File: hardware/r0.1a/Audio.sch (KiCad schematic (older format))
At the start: 76 parts, among them J4 MBIAS, J5 TX_Trim, J6 Kenwood-2.5, J7 Radio, J8 Kenwood-3.5, Q1 IRLML2060, U5 LM386, U6 MCP6002-xSN, U7 MCP6002-xSN, U8 LMV341

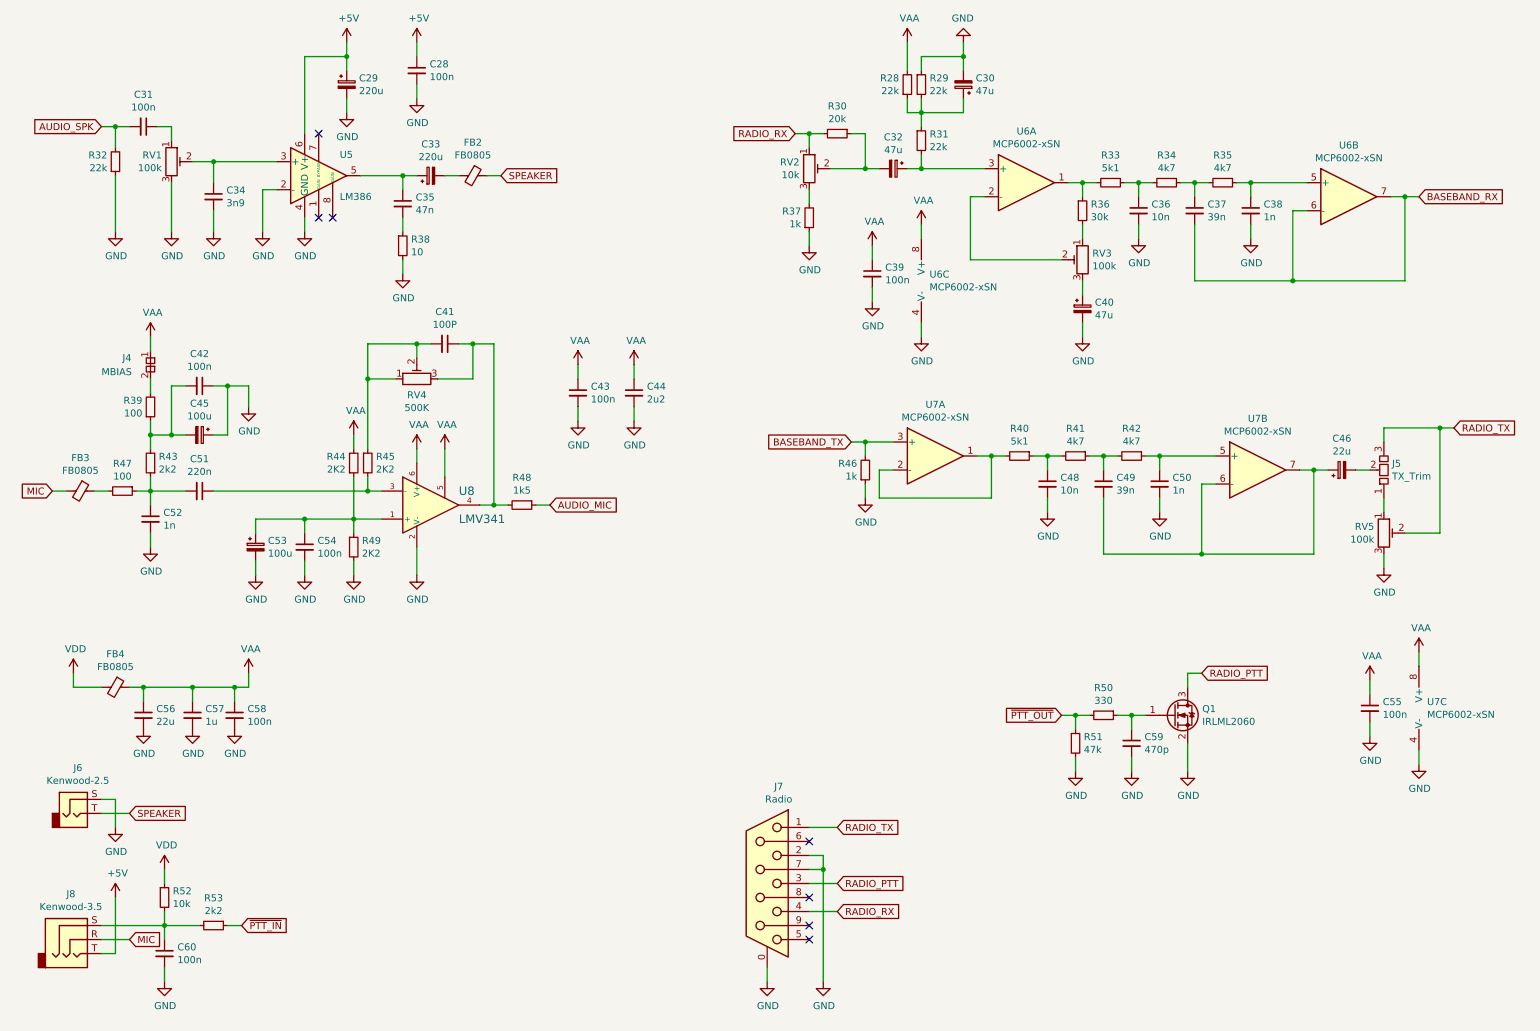
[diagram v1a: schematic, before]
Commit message: Small fixes / updates
* Fixed library path
* Added 12 MHz TCXO
* Replaced rotary encoder with more buttons
* Changed radio connector pinout to be compatible with Repeater Builder and BI7JTA modem boards
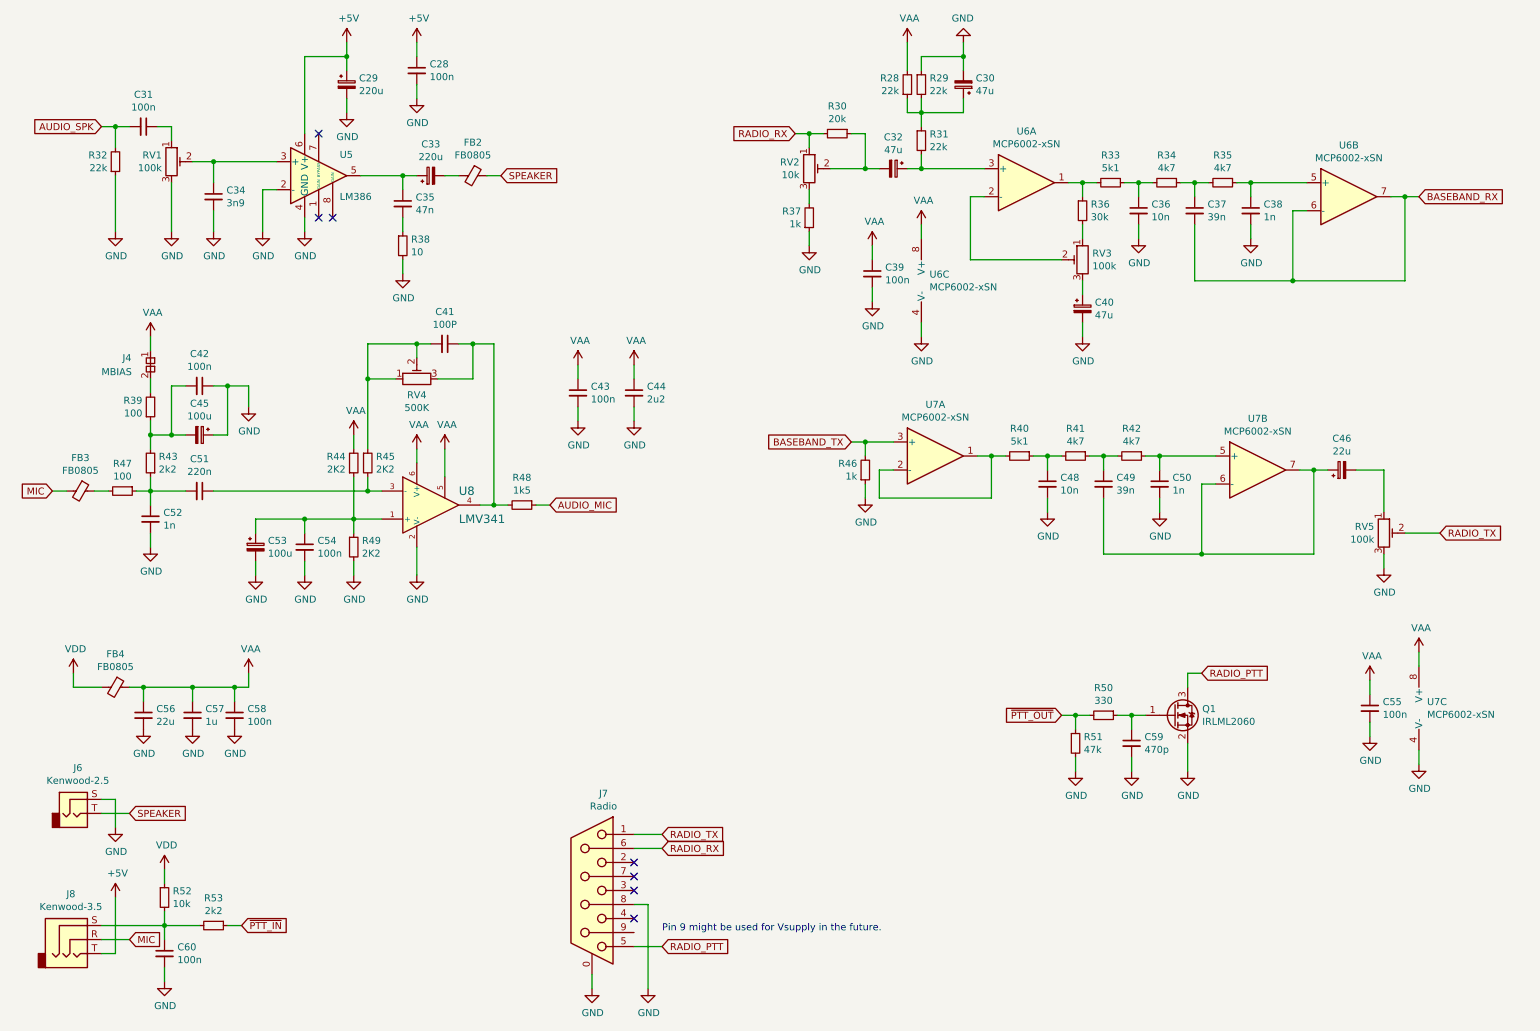
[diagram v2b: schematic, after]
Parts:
- removed J5: TX_Trim, symbol pkl_misc:pkl_double_jumper
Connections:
- net GND: now also J7.8; no longer J7.2, J7.7
- net RADIO_PTT: now also J7.5; no longer J7.3
- net RADIO_RX: now also J7.6; no longer J7.4
- net at C46.2: now also RV5.1
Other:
- note added: "Pin 9 might be used for Vsupply in the future."
- moved on the sheet: J7
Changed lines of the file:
@@
 	9750 3850 9850 3850
 Connection ~ 9750 3850
-Wire Wire Line
-	10050 3850 10150 3850
-$Comp
-L pkl_misc:pkl_double_jumper J5
-U 1 1 6210D6B9
-P 10250 3850
-F 0 "J5" V 10296 3792 50  0000 R CNN
-F 1 "TX_Trim" V 10205 3792 50  0000 R CNN
-F 2 "" H 10200 3850 50  0001 C CNN
-F 3 "" H 10200 3850 50  0001 C CNN
-	1    10250 3850
-	0    -1   -1   0
-$EndComp
 $Comp
 L Device:R_POT_TRIM RV5
@@
 	1    0    0    -1
 $EndComp
-Wire Wire Line
-	10250 4050 10250 4150
 $Comp
 L power:GND #PWR093
@@
 	10250 4550 10250 4450
 Wire Wire Line
-	10250 3650 10250 3550
-Wire Wire Line
-	10250 3550 10650 3550
-Wire Wire Line
-	10650 3550 10650 4300
-Wire Wire Line
 	10650 4300 10400 4300
-Wire Wire Line
-	10650 3550 10750 3550
-Connection ~ 10650 3550
-Text GLabel 10750 3550 2    50   Input ~ 0
+Text GLabel 10650 4300 2    50   Input ~ 0
 RADIO_TX
 $Comp
@@
 L Connector:DB9_Female_MountingHoles J7
 U 1 1 62239A82
-P 5850 6800
-F 0 "J7" H 5768 7492 50  0000 C CNN
-F 1 "Radio" H 5768 7401 50  0000 C CNN
-F 2 "" H 5850 6800 50  0001 C CNN
-F 3 " ~" H 5850 6800 50  0001 C CNN
-	1    5850 6800
+P 4600 6850
+F 0 "J7" H 4518 7542 50  0000 C CNN
+F 1 "Radio" H 4518 7451 50  0000 C CNN
+F 2 "" H 4600 6850 50  0001 C CNN
+F 3 " ~" H 4600 6850 50  0001 C CNN
+	1    4600 6850
 	-1   0    0    -1
 $EndComp
@@
 L power:GND #PWR0114
 U 1 1 62239ED8
-P 5850 7500
-F 0 "#PWR0114" H 5850 7250 50  0001 C CNN
-F 1 "GND" H 5855 7327 50  0000 C CNN
-F 2 "" H 5850 7500 50  0001 C CNN
-F 3 "" H 5850 7500 50  0001 C CNN
-	1    5850 7500
-	1    0    0    -1
-$EndComp
-Wire Wire Line
-	5850 7400 5850 7500
-Text GLabel 6350 6400 2    50   Input ~ 0
+P 4600 7550
+F 0 "#PWR0114" H 4600 7300 50  0001 C CNN
+F 1 "GND" H 4605 7377 50  0000 C CNN
+F 2 "" H 4600 7550 50  0001 C CNN
+F 3 "" H 4600 7550 50  0001 C CNN
+	1    4600 7550
+	1    0    0    -1
+$EndComp
+Wire Wire Line
+	4600 7450 4600 7550
+Text GLabel 5100 6450 2    50   Input ~ 0
 RADIO_TX
-Wire Wire Line
-	6150 6600 6250 6600
-Wire Wire Line
-	6250 6600 6250 6700
-Wire Wire Line
-	6250 6700 6150 6700
-Wire Wire Line
-	6250 6700 6250 7500
-Connection ~ 6250 6700
 $Comp
 L power:GND #PWR0115
 U 1 1 62267D15
-P 6250 7500
-F 0 "#PWR0115" H 6250 7250 50  0001 C CNN
-F 1 "GND" H 6255 7327 50  0000 C CNN
-F 2 "" H 6250 7500 50  0001 C CNN
-F 3 "" H 6250 7500 50  0001 C CNN
-	1    6250 7500
-	1    0    0    -1
-$EndComp
-NoConn ~ 6150 6500
-NoConn ~ 6150 6900
-NoConn ~ 6150 7100
-NoConn ~ 6150 7200
-Text GLabel 6350 6800 2    50   Input ~ 0
+P 5000 7550
+F 0 "#PWR0115" H 5000 7300 50  0001 C CNN
+F 1 "GND" H 5005 7377 50  0000 C CNN
+F 2 "" H 5000 7550 50  0001 C CNN
+F 3 "" H 5000 7550 50  0001 C CNN
+	1    5000 7550
+	1    0    0    -1
+$EndComp
+Text GLabel 5100 7250 2    50   Input ~ 0
 RADIO_PTT
-Wire Wire Line
-	6150 6400 6350 6400
-Text GLabel 6350 7000 2    50   Input ~ 0
+Text GLabel 5100 6550 2    50   Input ~ 0
 RADIO_RX
 Wire Wire Line
-	6350 7000 6150 7000
-Wire Wire Line
-	6350 6800 6150 6800
-Wire Wire Line
 	6850 800  6850 1000
+Wire Wire Line
+	10050 3850 10250 3850
+Wire Wire Line
+	10250 3850 10250 4150
+Wire Wire Line
+	4900 6950 5000 6950
+Wire Wire Line
+	5000 6950 5000 7550
+Wire Wire Line
+	4900 7250 5100 7250
+Wire Wire Line
+	4900 6550 5100 6550
+Wire Wire Line
+	4900 6450 5100 6450
+NoConn ~ 4900 6650
+NoConn ~ 4900 6750
+NoConn ~ 4900 6850
+NoConn ~ 4900 7050
+Text Notes 5100 7150 0    50   ~ 0
+Pin 9 might be used for Vsupply in the future.
 $EndSCHEMATC

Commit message: Replaced Xtal parallel R with series R
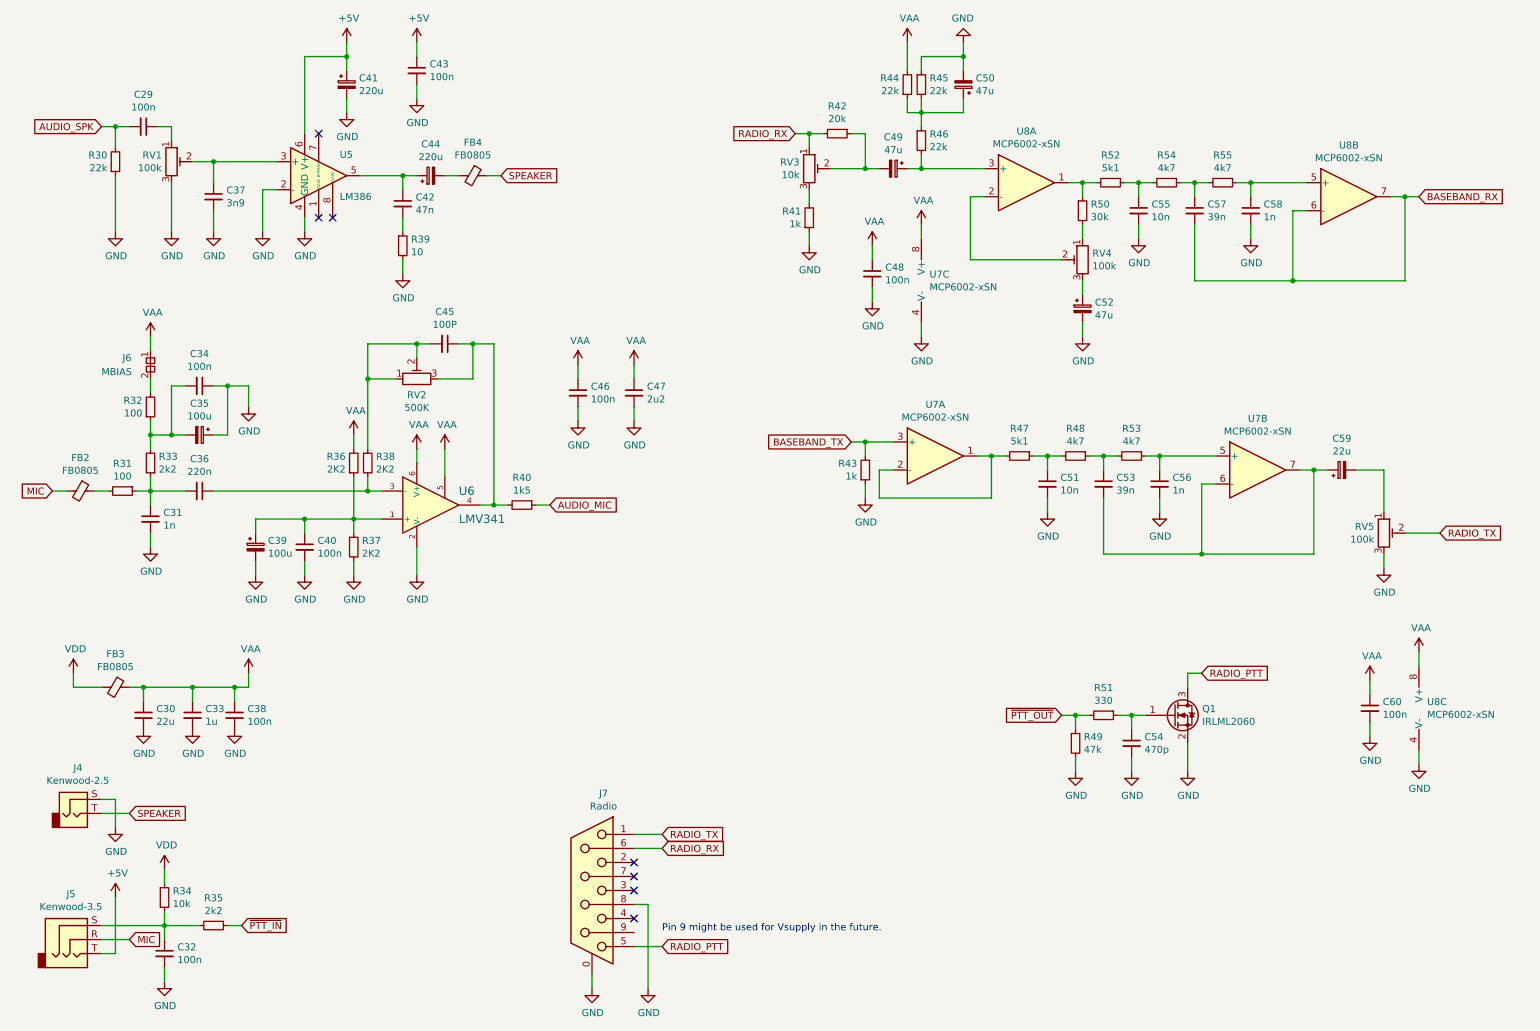
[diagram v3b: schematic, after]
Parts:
- renumbered C31 to C29, C56 to C30, C52 to C31, C60 to C32, C57 to C33, C42 to C34, C45 to C35, C51 to C36, C34 to C37, C58 to C38, C53 to C39, C54 to C40, C29 to C41, C35 to C42, C28 to C43, C33 to C44, C41 to C45, C43 to C46, C44 to C47, C39 to C48, C32 to C49, C30 to C50, C48 to C51, C40 to C52, C49 to C53, C59 to C54, C36 to C55, C50 to C56, C37 to C57, C38 to C58, C46 to C59, C55 to C60, FB3 to FB2, FB4 to FB3, FB2 to FB4, J6 to J4, J8 to J5, J4 to J6, R32 to R30, R47 to R31, R39 to R32, R43 to R33, R52 to R34, R53 to R35, R44 to R36, R49 to R37, R45 to R38, R38 to R39, R48 to R40, R37 to R41, R30 to R42, R46 to R43, R28 to R44, R29 to R45, R31 to R46, R40 to R47, R41 to R48, R51 to R49, R36 to R50, R50 to R51, R33 to R52, R42 to R53, R34 to R54, R35 to R55, RV4 to RV2, RV2 to RV3, RV3 to RV4, U8 to U6, U6 to U7, U6 to U8, U7 to U8
